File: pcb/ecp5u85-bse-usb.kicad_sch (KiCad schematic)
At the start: 32 parts, among them J1 Conn_02x40_Odd_Even, J2 Conn_02x40_Odd_Even, Q1 2N2222, U10 SiT9120AC-2C2-25E100.000000X

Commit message: Initial footprint assignment
- Some edits to the schematic to improve readability
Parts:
- removed Q1: 2N2222, symbol ecp5u85-bse-usb:2N2222
- removed R21: 10K, symbol Device:R_US
- C1: renamed from C130; footprint (none) -> Capacitor_SMD:C_0402_1005Metric
- C2: renamed from C131; footprint (none) -> Capacitor_SMD:C_0805_2012Metric
- C3: renamed from C132; footprint (none) -> Capacitor_SMD:C_1210_3225Metric
- D1: renamed from D3; footprint (none) -> LED_SMD:LED_0603_1608Metric
- D2: renamed from D4; footprint (none) -> LED_SMD:LED_0603_1608Metric
- D3: renamed from D5; footprint (none) -> LED_SMD:LED_0603_1608Metric
- D4: renamed from D6; footprint (none) -> LED_SMD:LED_0603_1608Metric
- D5: renamed from D7; footprint (none) -> LED_SMD:LED_0603_1608Metric
- D6: renamed from D8; footprint (none) -> LED_SMD:LED_0603_1608Metric
- D7: renamed from D9; footprint (none) -> LED_SMD:LED_0603_1608Metric
- J1, J2: value Conn_02x40_Odd_Even -> BSE-040-01-X-D-A; footprint (none) -> jonnew:SAMTEC_BSE-040-01-X-D-A
- R1: renamed from R56; footprint (none) -> Resistor_SMD:R_0402_1005Metric
- R10: renamed from R30; footprint (none) -> Resistor_SMD:R_0402_1005Metric
- R11: renamed from R19; footprint (none) -> Resistor_SMD:R_0402_1005Metric
- R12: renamed from R20; value 1.6k -> 4.7k; footprint (none) -> Resistor_SMD:R_0402_1005Metric
- R13: renamed from R22; footprint (none) -> Resistor_SMD:R_0402_1005Metric
- R14: renamed from R27; footprint (none) -> Resistor_SMD:R_0402_1005Metric
- R15: renamed from R31; footprint (none) -> Resistor_SMD:R_0402_1005Metric
- R16: renamed from R32; footprint (none) -> Resistor_SMD:R_0402_1005Metric
- R17: renamed from R33; footprint (none) -> Resistor_SMD:R_0402_1005Metric
- R2: renamed from R55; footprint (none) -> Resistor_SMD:R_0402_1005Metric
- R3: renamed from R57; footprint (none) -> Resistor_SMD:R_0402_1005Metric
- R4: renamed from R24; footprint (none) -> Resistor_SMD:R_0402_1005Metric
- R5: renamed from R26; footprint (none) -> Resistor_SMD:R_0402_1005Metric
- R6: renamed from R29; footprint (none) -> Resistor_SMD:R_0402_1005Metric
- R7: renamed from R23; footprint (none) -> Resistor_SMD:R_0402_1005Metric
- R8: renamed from R25; footprint (none) -> Resistor_SMD:R_0402_1005Metric
- R9: renamed from R28; footprint (none) -> Resistor_SMD:R_0402_1005Metric
- U1: renamed from U10; footprint (none) -> jonnew:SITIME_LGA6-5x3.2x0.75
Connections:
- net DONE: now also D2.1 (K)
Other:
- sheet FPGA ports: added FT_RST_{Req}; removed ~{FT_RESET}
- sheet FTDI ports: added FT_RST_{Req}; removed ~{FT_RESET}
- company: OEPS -> OEPS & Open Ephys, Inc.
- title: ECP5U85-BSE-USB Breakout board -> ECP5U85-BSE-USB Breakout Board
- moved on the sheet: D2, R12

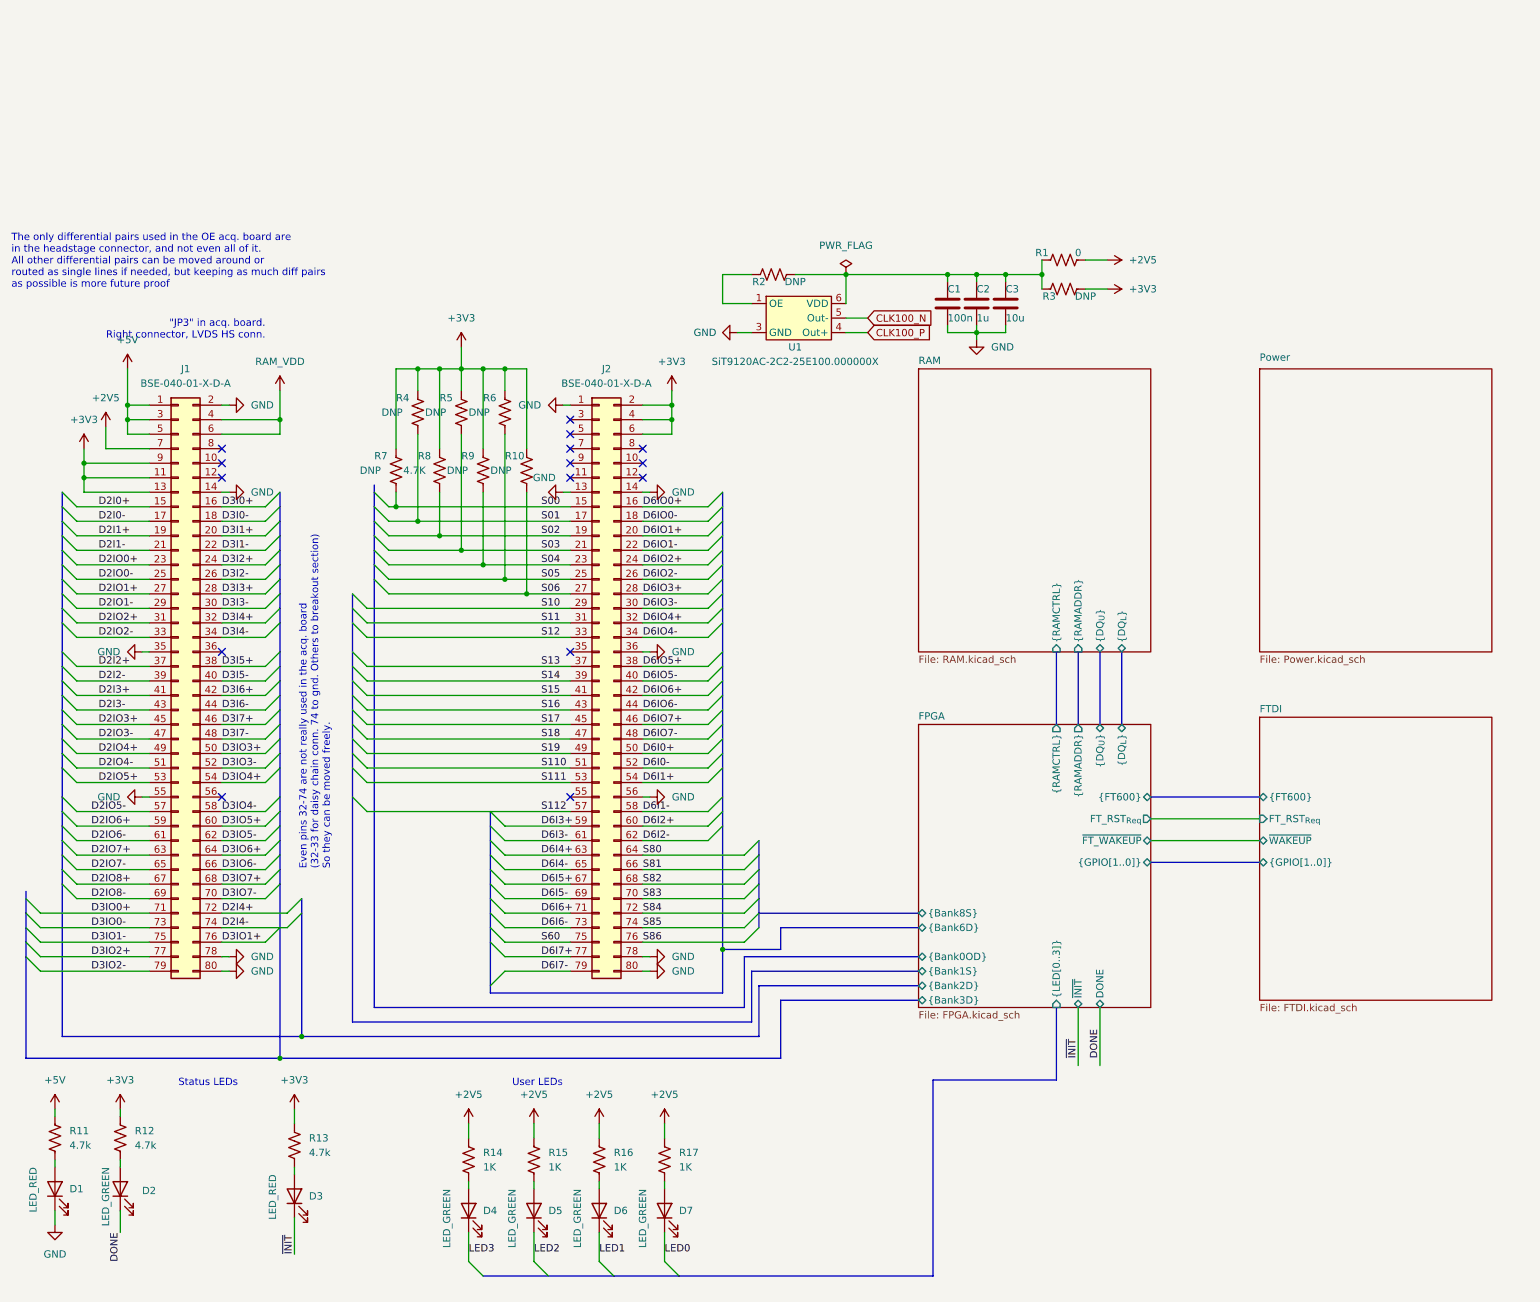
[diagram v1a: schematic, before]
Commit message: Rough PCB component placement
- This will change
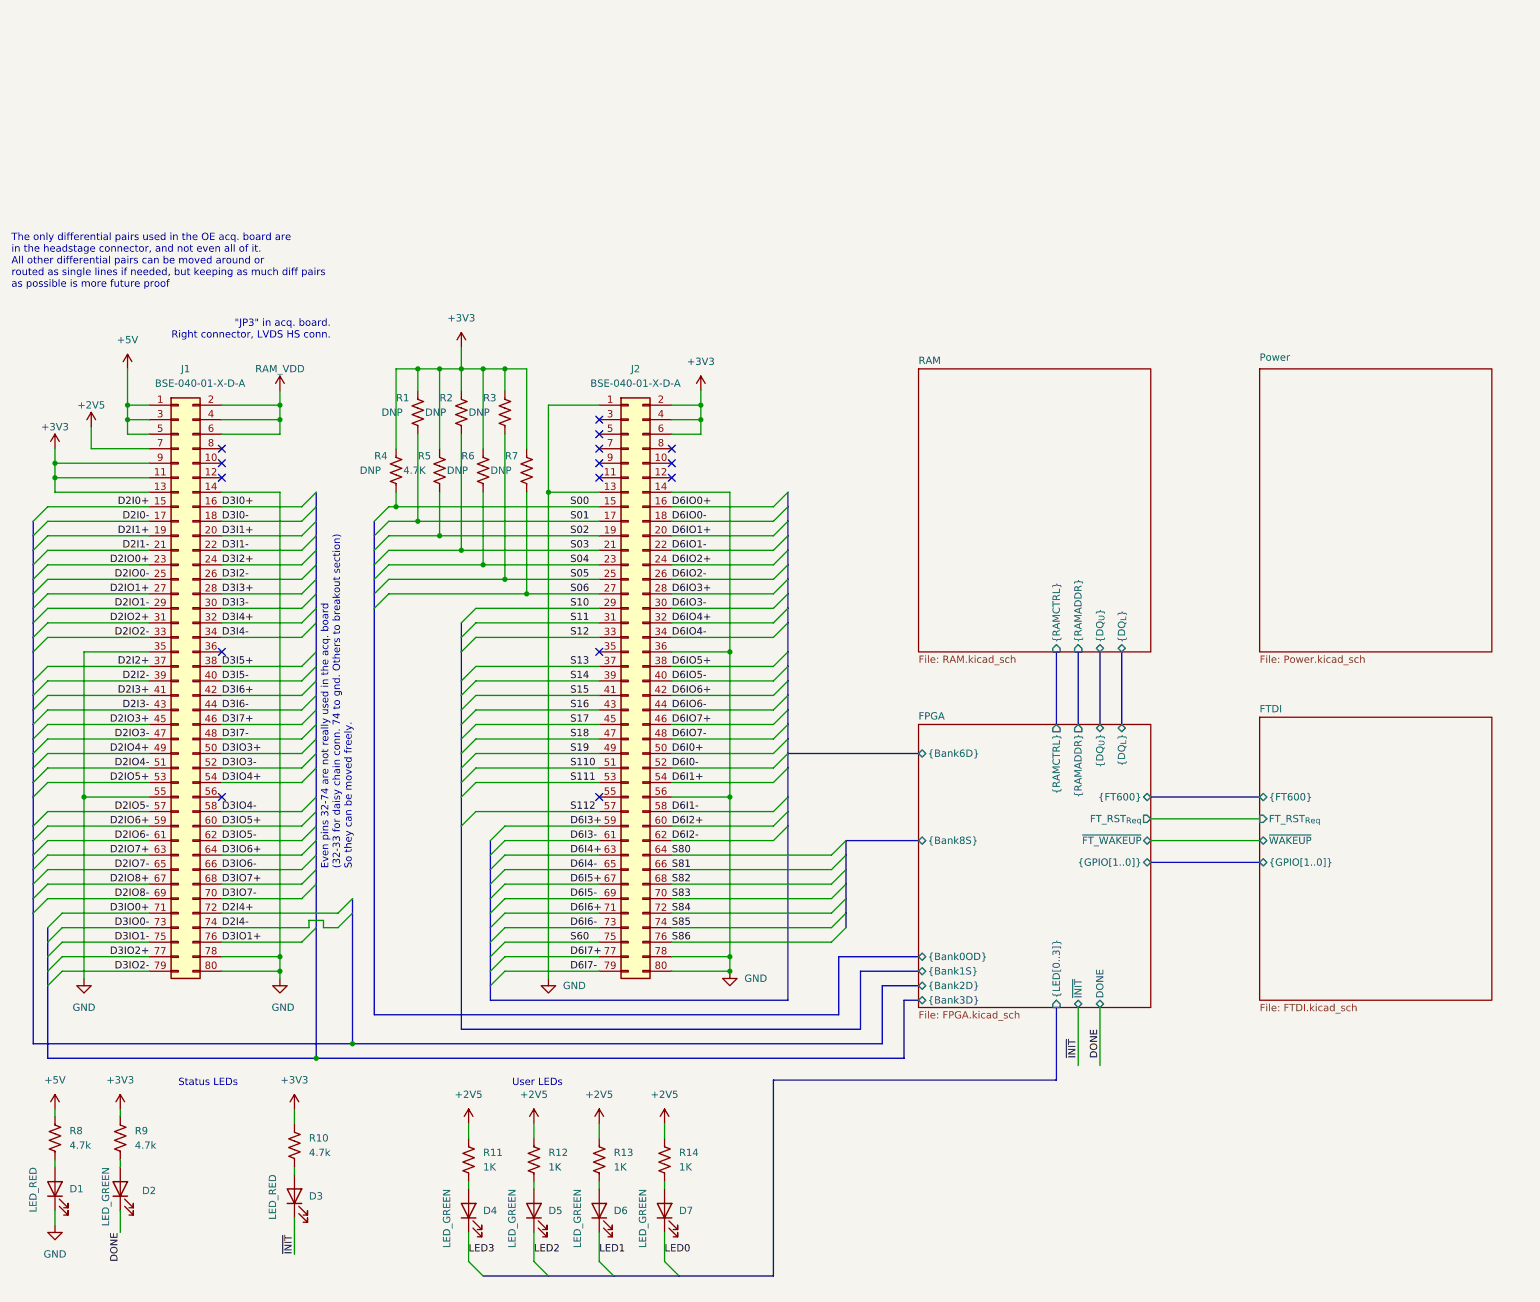
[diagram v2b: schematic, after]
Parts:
- removed C1: 100n, Capacitor_SMD:C_0402_1005Metric, symbol Device:C
- removed C2: 1u, Capacitor_SMD:C_0805_2012Metric, symbol Device:C
- removed C3: 10u, Capacitor_SMD:C_1210_3225Metric, symbol Device:C
- removed R1: 0, Resistor_SMD:R_0402_1005Metric, symbol Device:R_US
- removed R2, R3: DNP, Resistor_SMD:R_0402_1005Metric, symbol Device:R_US
- removed U1: SiT9120AC-2C2-25E100.000000X, jonnew:SITIME_LGA6-5x3.2x0.75, symbol ecp5u85-bse-usb:OSCILLATOR_DIFF
- renumbered R4 to R1, R13 to R10, R14 to R11, R15 to R12, R16 to R13, R17 to R14, R5 to R2, R6 to R3, R7 to R4, R8 to R5, R9 to R6, R10 to R7, R11 to R8, R12 to R9
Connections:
- net GND: no longer J1.2 (Pin_2)
- net RAM_VDD: now also J1.2 (Pin_2)
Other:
- moved on the sheet: J2

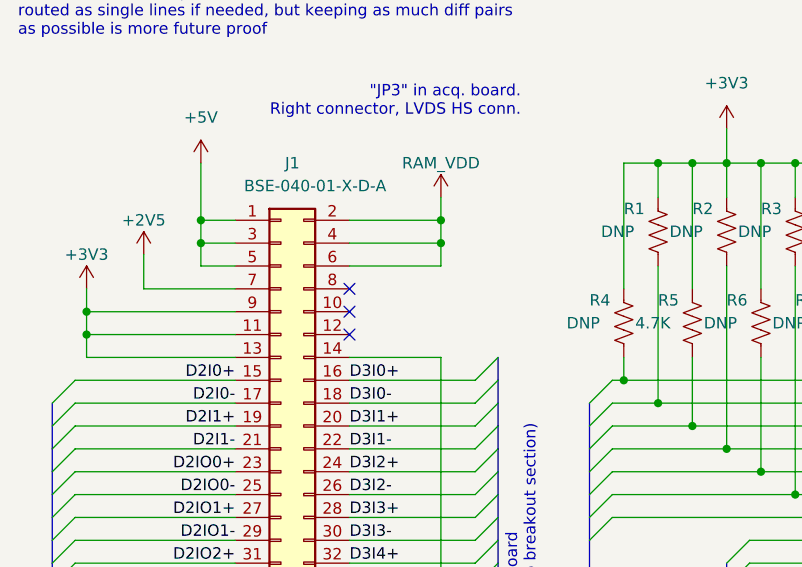
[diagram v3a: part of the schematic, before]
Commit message: Return RAM UDQS signals to dedicated FPGA pin
- J1.2 moved to ground instead of RAM_VDD
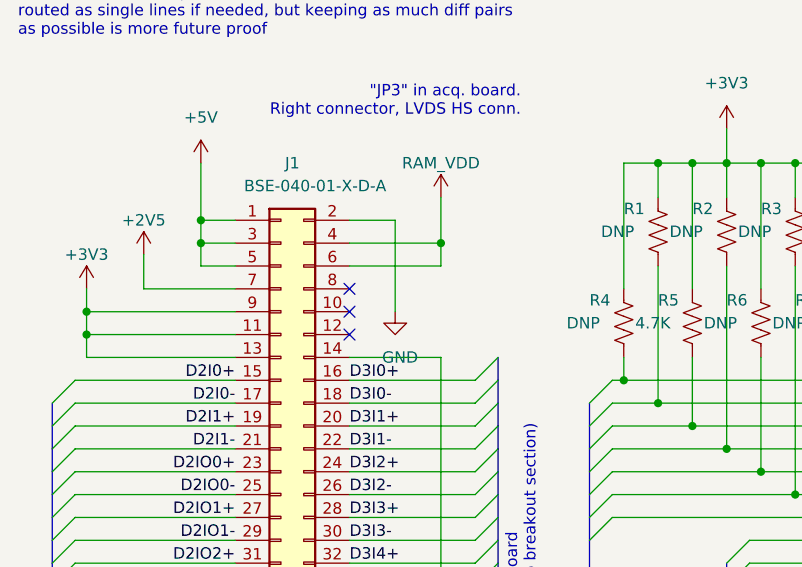
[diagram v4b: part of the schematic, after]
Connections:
- net GND: now also J1.2 (Pin_2)
- net RAM_VDD: no longer J1.2 (Pin_2)
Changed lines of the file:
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@@
   (junction (at 21.59 55.88) (diameter 0) (color 0 0 0 0)
   )
-  (junction (at 60.96 43.18) (diameter 0) (color 0 0 0 0)
-  )
   (junction (at 104.14 76.2) (diameter 0) (color 0 0 0 0)
   )
@@
     (stroke (width 0) (type default) (color 0 0 0 0))
   )
-  (wire (pts (xy 60.96 40.64) (xy 60.96 43.18))
-    (stroke (width 0) (type default) (color 0 0 0 0))
-  )
   (wire (pts (xy 96.52 36.83) (xy 100.33 36.83))
     (stroke (width 0) (type default) (color 0 0 0 0))
@@
     (stroke (width 0) (type default) (color 0 0 0 0))
   )
-  (wire (pts (xy 50.8 43.18) (xy 60.96 43.18))
-    (stroke (width 0) (type default) (color 0 0 0 0))
-  )
   (wire (pts (xy 107.95 43.18) (xy 107.95 58.42))
     (stroke (width 0) (type default) (color 0 0 0 0))
@@
     (stroke (width 0) (type default) (color 0 0 0 0))
   )
+  (wire (pts (xy 55.88 53.34) (xy 55.88 43.18))
+    (stroke (width 0) (type default) (color 0 0 0 0))
+  )
   (wire (pts (xy 134.62 45.72) (xy 134.62 43.18))
     (stroke (width 0) (type default) (color 0 0 0 0))
@@
     (stroke (width 0) (type default) (color 0 0 0 0))
   )
-  (wire (pts (xy 60.96 43.18) (xy 60.96 45.72))
+  (wire (pts (xy 60.96 40.64) (xy 60.96 45.72))
     (stroke (width 0) (type default) (color 0 0 0 0))
   )
@@
     (stroke (width 0) (type default) (color 0 0 0 0))
   )
+  (wire (pts (xy 50.8 43.18) (xy 55.88 43.18))
+    (stroke (width 0) (type default) (color 0 0 0 0))
+  )
   (wire (pts (xy 50.8 104.14) (xy 64.77 104.14))
     (stroke (width 0) (type default) (color 0 0 0 0))
@@
     (pin "1")
   )
+  (symbol (lib_id "power:GND") (at 55.88 53.34 0) (unit 1)
+    (in_bom yes) (on_board yes)
+    (property "Reference" "#PWR?" (id 0) (at 55.88 59.69 0)
+      (effects (font (size 1.27 1.27)) hide)
+    )
+    (property "Value" "GND" (id 1) (at 58.42 58.42 0)
+      (effects (font (size 1.27 1.27)) (justify right))
+    )
+    (property "Footprint" "" (id 2) (at 55.88 53.34 0)
+      (effects (font (size 1.27 1.27)) hide)
+    )
+    (property "Datasheet" "" (id 3) (at 55.88 53.34 0)
+      (effects (font (size 1.27 1.27)) hide)
+    )
+    (pin "1")
+  )
   (symbol (lib_id "power:GND") (at 139.7 142.24 0) (unit 1)
     (in_bom yes) (on_board yes) (fields_autoplaced)
@@
       (reference "#PWR0122") (unit 1) (value "GND") (footprint "")
     )
+    (path "/75998b3e-9bf5-4a61-af4c-5cc161435e05"
+      (reference "#PWR?") (unit 1) (value "GND") (footprint "")
+    )
     (path "/b14c35da-dd14-4b8d-93a9-00f219a92f41/a6521404-6cfd-4ad4-b208-dc50164c9ef1"
